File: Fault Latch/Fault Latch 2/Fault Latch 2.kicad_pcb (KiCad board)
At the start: 2 copper layers, 123 x 100 mm, 101 parts, among them K101 Fujitsu_FTR-LYAA005x, K102 Fujitsu_FTR-LYAA005x, K103 Fujitsu_FTR-LYAA005x, Q102 Q_NMOS_GSD, Q104 Q_NPN_BEC, Q105 Q_PMOS_GSD, Q106 Q_NPN_BEC, Q107 Q_NPN_BEC, Q108 Q_NPN_BEC, Q109 Q_NMOS_GDS, Q110 Q_NMOS_GDS, Q111 Q_NMOS_GDS, Q112 Q_NPN_BEC, Q113 Q_NPN_BEC, Q114 Q_NMOS_GSD, Q115 Q_NMOS_GSD, SW101 SW_Omron_B3FS, SW102 SW_Omron_B3FS, SW103 SW_Omron_B3FS, U101 641964-1, U102 74AHC1G00, U103 74AHC1G00, U104 74AHC1G00, U105 641964-1, U106 74LS279, U110 641964-1, U111 641964-1, U112 641964-1, U113 641964-1, U114 SFH617A-1, U115 SFH617A-1, U116 SFH617A-1, U117 74AHC1G32, U118 LM555xM, U119 641964-1, U120 74AHC1G08, U121 641964-1, U122 641964-1

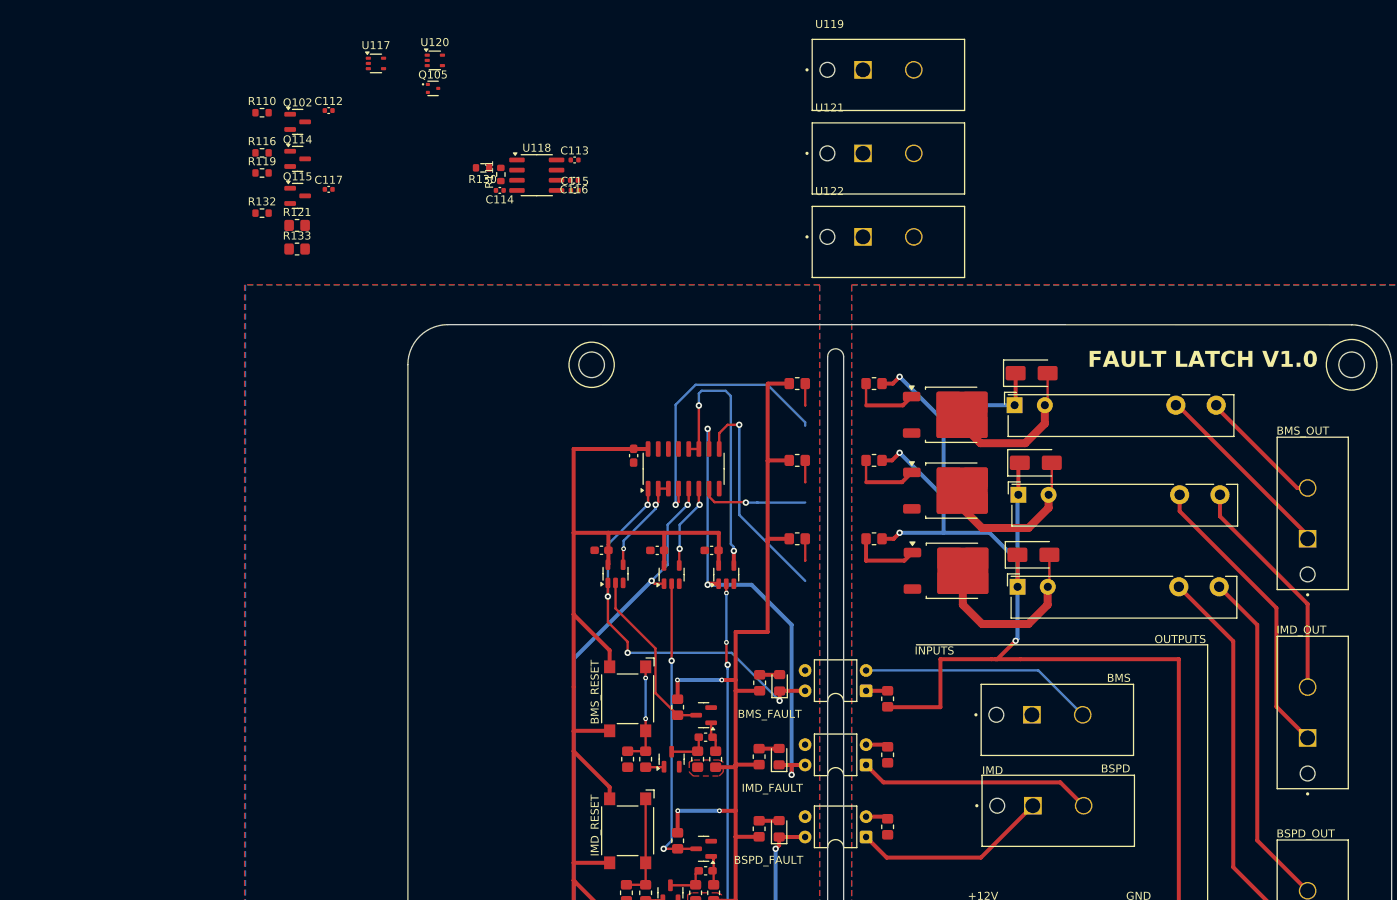
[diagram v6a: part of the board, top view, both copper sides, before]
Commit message: FIXED PMOS
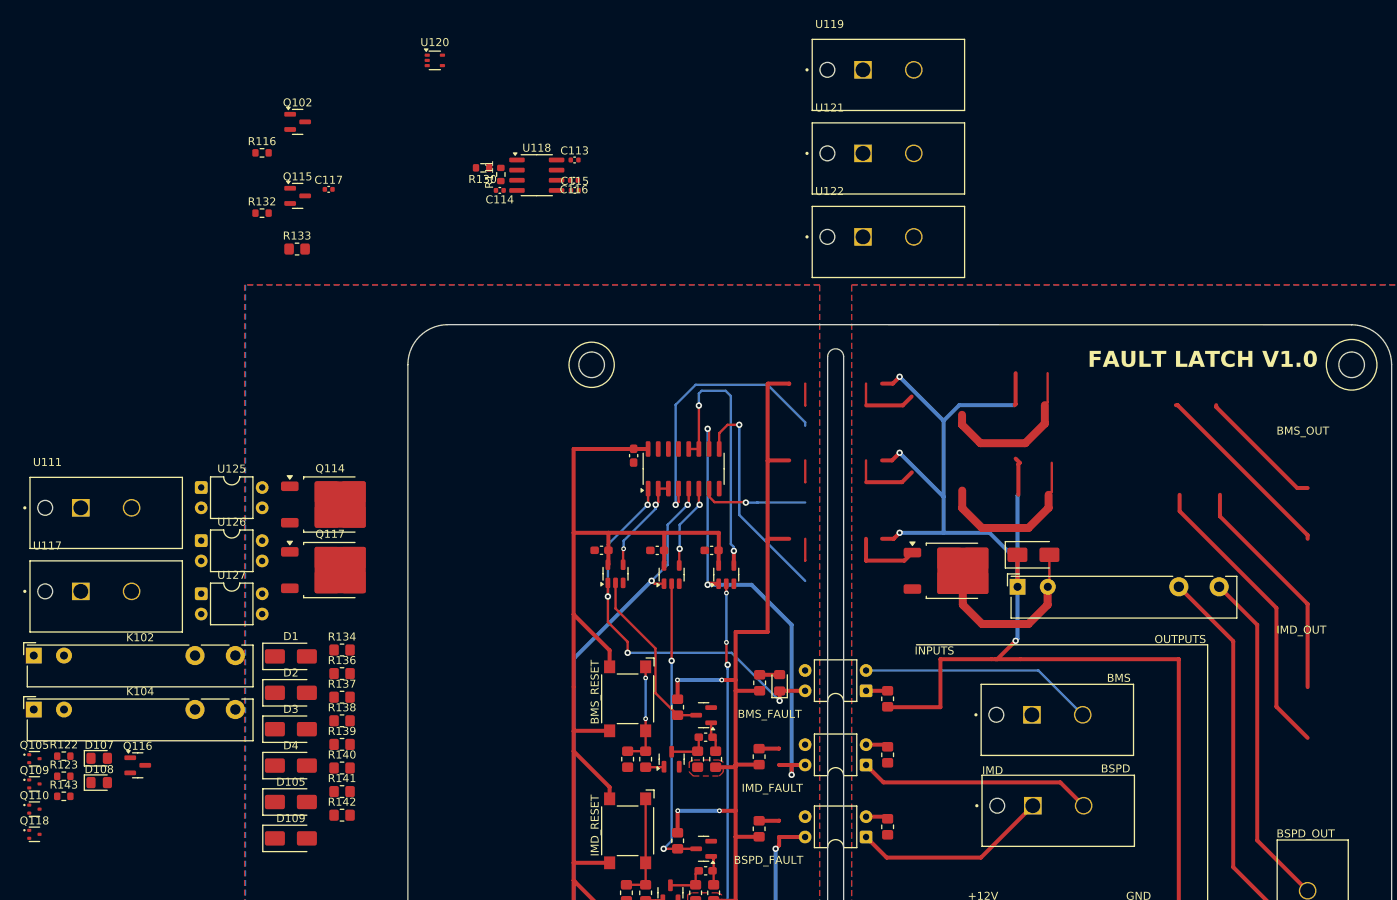
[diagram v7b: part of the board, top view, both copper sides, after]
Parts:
- removed C112: 0.1u, Capacitor_SMD:C_0402_1005Metric
- removed D101, D102: RED, LED_SMD:LED_0805_2012Metric_Pad1.15x1.40mm_HandSolder
- removed D104: D_Schottky, Diode_SMD:D_SMA
- removed K101: Fujitsu_FTR-LYAA005x, Relay_THT:Relay_SPST-NO_Fujitsu_FTR-LYAA005x_FormA_Vertical
- removed R110: 1k, Resistor_SMD:R_0603_1608Metric
- removed the R116 at (105.7, 57.4)
- removed R117, R118, R121: 270R, Resistor_SMD:R_0805_2012Metric_Pad1.20x1.40mm_HandSolder
- removed R119: 10k, Resistor_SMD:R_0603_1608Metric
- removed R121: 10k, Resistor_SMD:R_0805_2012Metric_Pad1.20x1.40mm_HandSolder
- removed U110: 641964-1, 641964-1:TE_641964-1
- added D1: US2AA, Diode_SMD:D_SMA, F.Cu at (42.4, 91.5)
- added D107: RED, LED_SMD:LED_0805_2012Metric_Pad1.15x1.40mm_HandSolder, F.Cu at (18.4, 104.2)
- added D108: RED, LED_SMD:LED_0805_2012Metric_Pad1.15x1.40mm_HandSolder, F.Cu at (18.4, 107.2)
- added D109: D_Schottky, Diode_SMD:D_SMA, F.Cu at (42.4, 114.2)
- added D2: US2AA, Diode_SMD:D_SMA, F.Cu at (42.4, 96.0)
- added D3: US2AA, Diode_SMD:D_SMA, F.Cu at (42.4, 100.5)
- added D4: US2AA, Diode_SMD:D_SMA, F.Cu at (42.4, 105.1)
- added K104: Fujitsu_FTR-LYAA005x, Relay_THT:Relay_SPST-NO_Fujitsu_FTR-LYAA005x_FormA_Vertical, F.Cu at (10.3, 98.1)
- added Q116: Q_NMOS_GSD, Package_TO_SOT_SMD:SOT-23, F.Cu at (23.3, 105.1)
- added Q117: Q_NMOS_GDS, Package_TO_SOT_SMD:TO-252-2, F.Cu at (47.3, 80.7)
- added Q118: Q_PMOS_GSD, Package_TO_SOT_SMD:SOT-523, F.Cu at (10.3, 113.7)
- added R134: 270R, Resistor_SMD:R_0805_2012Metric_Pad1.20x1.40mm_HandSolder, F.Cu at (48.8, 90.7)
- added R136: 270R, Resistor_SMD:R_0805_2012Metric_Pad1.20x1.40mm_HandSolder, F.Cu at (48.8, 93.6)
- added R137: 10k, Resistor_SMD:R_0805_2012Metric_Pad1.20x1.40mm_HandSolder, F.Cu at (48.8, 96.5)
- added R138: 10k, Resistor_SMD:R_0805_2012Metric_Pad1.20x1.40mm_HandSolder, F.Cu at (48.8, 99.5)
- added R139: 10k, Resistor_SMD:R_0805_2012Metric_Pad1.20x1.40mm_HandSolder, F.Cu at (48.8, 102.5)
- added R140: 10k, Resistor_SMD:R_0805_2012Metric_Pad1.20x1.40mm_HandSolder, F.Cu at (48.8, 105.4)
- added R141: 10k, Resistor_SMD:R_0805_2012Metric_Pad1.20x1.40mm_HandSolder, F.Cu at (48.8, 108.3)
- added R142: 10k, Resistor_SMD:R_0805_2012Metric_Pad1.20x1.40mm_HandSolder, F.Cu at (48.8, 111.3)
- added R143: 10k, Resistor_SMD:R_0603_1608Metric, F.Cu at (14.0, 108.9)
- added U125: SFH617A-1, Package_DIP:DIP-4_W7.62mm, F.Cu at (31.2, 70.3)
- added U126: SFH617A-1, Package_DIP:DIP-4_W7.62mm, F.Cu at (31.2, 77.0)
- added U127: SFH617A-1, Package_DIP:DIP-4_W7.62mm, F.Cu at (31.2, 83.6)
- Q109, Q110: value Q_NMOS_GDS -> Q_PMOS_GSD; footprint Package_TO_SOT_SMD:TO-252-2 -> Package_TO_SOT_SMD:SOT-523
- Q114: value Q_NMOS_GSD -> Q_NMOS_GDS; footprint Package_TO_SOT_SMD:SOT-23 -> Package_TO_SOT_SMD:TO-252-2
- R104, R105, R107: value 270R -> 10k
- R122: value 10k -> 270R; footprint Resistor_SMD:R_0805_2012Metric_Pad1.20x1.40mm_HandSolder -> Resistor_SMD:R_0603_1608Metric
- R123: footprint Resistor_SMD:R_0805_2012Metric_Pad1.20x1.40mm_HandSolder -> Resistor_SMD:R_0603_1608Metric
- R132: value 1k -> 10k
- U117: value 74AHC1G32 -> 641964-1; footprint Package_TO_SOT_SMD:SOT-353_SC-70-5 -> 641964-1:TE_641964-1
- moved U111 156.0 mm to (16.1, 72.9), turned to 0 degrees
- moved K102 124.7 mm to (10.3, 91.3)
- moved Q109 123.6 mm to (10.3, 107.4)
- moved Q110 121.4 mm to (10.3, 110.5)
- moved R122 107.8 mm to (14.0, 103.9)
- moved R123 105.5 mm to (14.0, 106.4)
- moved D105 102.3 mm to (42.4, 109.7)
- moved Q105 97.5 mm to (10.3, 104.2)
- moved U117 75.6 mm to (16.1, 83.3)
- moved Q114 43.4 mm to (47.3, 72.5)
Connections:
- D103 pad 1: /NBMS_LV -> Net-(D103-K)
- D105 pad 1: +5V -> /IMD_SR
- D105 pad 2: Net-(D105-A) -> GND
- K102 pad A1: +5V -> /IMD_SR
- K102 pad A2: Net-(D105-A) -> GND
- Q102 pad 1: +5V -> /IMD_LED
- Q105 pad 1: Net-(Q105-G) -> Net-(D107-K)
- Q105 pad 3: +12V -> +5V
- Q109 pad 1: Net-(Q109-G) -> Net-(D103-K)
- Q109 pad 3: GNDPWR -> +5V
- Q110 pad 1: Net-(Q110-G) -> /BMS_SR
- Q110 pad 2: Net-(D105-A) -> Net-(D3-A)
- Q110 pad 3: GNDPWR -> +5V
- Q111 pad 1: Net-(Q111-G) -> Net-(D108-K)
- Q111 pad 3: GNDPWR -> GND
- Q114 pad 1: Net-(Q105-S) -> Net-(Q114-G)
- Q114 pad 2: GND -> /IMD_Green
- Q114 pad 3: Net-(Q114-D) -> GNDPWR
- Q115 pad 2: GND -> GNDPWR
- R104 pad 2: Net-(D101-A) -> /NIMD_LV
- R105 pad 2: Net-(D102-A) -> /NBPSD_LV
- R107 pad 2: Net-(D103-A) -> /NBMS_LV
- R116 pad 1: +5V -> +12V
- R122 pad 1: Net-(Q110-G) -> Net-(R122-Pad1)
- R123 pad 1: Net-(Q111-G) -> GNDPWR
- R123 pad 2: +12V -> Net-(D1-K)
- R132 pad 1: Net-(Q115-G) -> Net-(R132-Pad1)
- R132 pad 2: GND -> Net-(R132-Pad2)
- R133 pad 1: Net-(Q109-G) -> Net-(D103-A)
- U106 pad 4: Net-(Q109-G) -> Net-(D103-K)
- U106 pad 7: Net-(Q110-G) -> Net-(D107-K)
- U106 pad 9: Net-(Q111-G) -> Net-(D108-K)
- U117 pad 1: +5V -> Net-(K104-Pad13)
- U117 pad 2: +5V -> Net-(K104-Pad14)
- U119 pad 1: GND -> Net-(Q116-D)
- U119 pad 2: Net-(Q105-S) -> Net-(R122-Pad1)
- U120 pad 1: Net-(Q114-D) -> Net-(D3-K)
- U120 pad 4: Net-(Q115-G) -> Net-(R132-Pad1)
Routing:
- net (no net): track 0.00 -> 106.4 mm
- net Net-(Q109-G): track 43.1 -> 0.00 mm, vias 1 -> 0
- net Net-(Q111-G): track 39.5 -> 0.00 mm, vias 1 -> 0
- net Net-(D108-K): track 0.00 -> 36.8 mm, vias 0 -> 1
- net Net-(D103-K): track 0.00 -> 34.3 mm, vias 0 -> 1
- net Net-(K101-Pad13): track 23.6 -> 0.00 mm
- net Net-(Q110-G): track 22.3 -> 0.00 mm, vias 1 -> 0
- net Net-(D105-A): track 20.9 -> 0.00 mm
- net Net-(Q109-S): track 20.0 -> 0.00 mm
- net Net-(K101-Pad14): track 15.8 -> 0.00 mm
- net Net-(D107-K): track 0.00 -> 13.3 mm, vias 0 -> 1
- net Net-(R116-Pad1): track 2.73 -> 0.00 mm
- net Net-(R117-Pad1): track 2.73 -> 0.00 mm
- net /NIMD_LV: track 112.3 -> 114.8 mm
- net Net-(D101-A): track 2.51 -> 0.00 mm
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
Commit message: Fault Latch V2.0 Prototype
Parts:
- moved R116 137.1 mm to (128.9, 131.9), turned to -90 degrees
- moved Q102 135.9 mm to (125.3, 133.0)
- moved U117 128.1 mm to (138.7, 46.1)
- moved U111 123.4 mm to (138.6, 57.6)
- moved U120 122.5 mm to (91.3, 135.5)
- moved R122 116.0 mm to (129.9, 109.8), turned to -90 degrees
- moved R132 115.3 mm to (93.1, 137.7)
- moved C114 113.8 mm to (92.4, 144.5), turned to -90 degrees
- moved C116 113.3 mm to (101.3, 142.8)
- moved C115 113.3 mm to (101.4, 144.0)
- moved U118 113.3 mm to (96.6, 142.1)
- moved R111 113.3 mm to (92.1, 142.0)
- moved C113 112.7 mm to (100.8, 139.7), turned to 90 degrees
- moved R130 112.2 mm to (91.4, 139.8)
- moved C117 109.9 mm to (91.8, 133.5), turned to 180 degrees
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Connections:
- Q102 pad 2: GND -> GNDPWR
- Q117 pad 2: /IMD_Green -> /BMS_Green
- R140 pad 2: /IMD_Green -> /BMS_Green
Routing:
- net +12V: track 236.5 -> 124.5 mm, vias 4 -> 5
- net /IMD_SR: track 0.00 -> 110.8 mm, vias 0 -> 4
- net /BMS_SR: track 0.00 -> 110.3 mm, vias 0 -> 6
- net (no net): track 106.4 -> 0.00 mm
- net /NIMD_LV: track 114.8 -> 46.4 mm, vias 3 -> 2
- net Net-(R132-Pad2): track 0.00 -> 68.1 mm, vias 0 -> 3
- net Net-(D108-K): track 36.8 -> 93.0 mm, vias 1 -> 0
- net /IMD_LED: track 0.00 -> 47.0 mm, vias 0 -> 2
- net Net-(Q115-D): track 0.00 -> 42.1 mm, vias 0 -> 1
- net Net-(Q102-D): track 0.00 -> 37.0 mm
- net Net-(D3-K): track 0.00 -> 32.6 mm
- net Net-(K103-Pad13): track 51.0 -> 18.7 mm
- net Net-(D107-K): track 13.3 -> 42.4 mm, vias 1 -> 2
- net Net-(Q117-G): track 0.00 -> 27.8 mm, vias 0 -> 2
- net Net-(K103-Pad14): track 42.6 -> 19.8 mm
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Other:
- board size 123 x 100 mm -> 351.1 x 116.3 mm
- board text added: "12+"
- board text added: "IMD LIGHT"
- board text added: "TSSI GREEN"
- board text added: "TSSI RED"
- board text added: "X"
- board text removed: "INPUTS"
- board text removed: "OUTPUTS"
